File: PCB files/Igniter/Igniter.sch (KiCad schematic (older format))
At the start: 23 parts, among them IC1 74HC4050, J1 PT, J13 Micro_SD_Card, J2 PT, J3 PT, J4 PT, J5 Battery, J6 Ignition Coil +, J7 Ignition coil -, Q1 N MOSFET, SW1 ARM

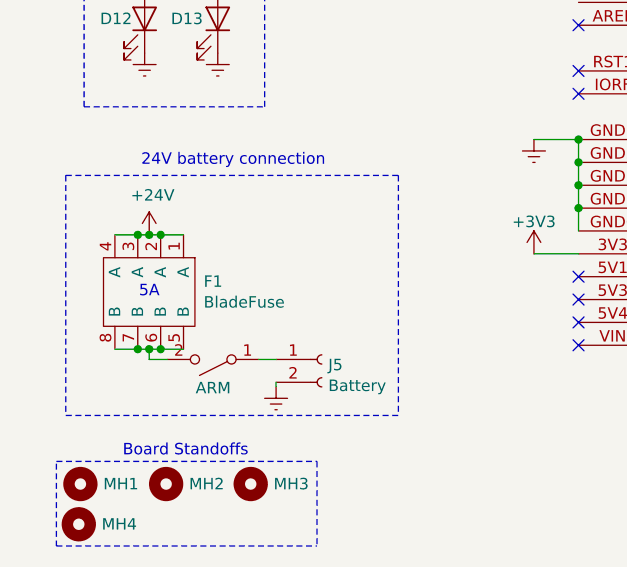
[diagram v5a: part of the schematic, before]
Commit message: 12/17/2019
-Board layout changes to make better routing paths, no traces drawn yet
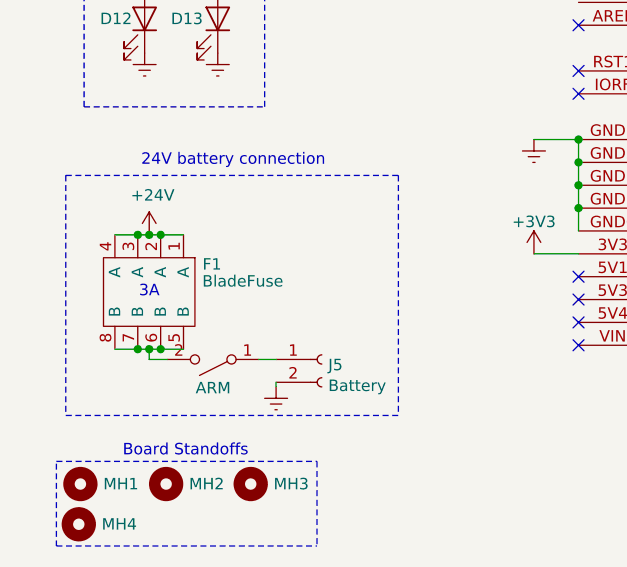
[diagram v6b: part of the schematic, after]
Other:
- note added: "3A"
- note removed: "5A"
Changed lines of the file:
@@
 	1526 7104 1601 7104
 Text Notes 1001 6839 0    50   ~ 0
-5A
-$Comp
-L power:+24V #PWR01
-U 1 1 5DBB64EE
-P 1046 6559
-F 0 "#PWR01" H 1046 6409 50  0001 C CNN
-F 1 "+24V" H 1061 6732 50  0000 C CNN
-F 2 "" H 1046 6559 50  0001 C CNN
-F 3 "" H 1046 6559 50  0001 C CNN
-	1    1046 6559
-	1    0    0    -1
-$EndComp
+3A
 $Comp
 L power:+24V #PWR08
@@
 U 1 1 5DCA7861
 P 1196 6809
-F 0 "F1" V 1150 6897 50  0000 L CNN
-F 1 "BladeFuse" V 1241 6897 50  0000 L CNN
+F 0 "F1" V 1075 6892 50  0000 L CNN
+F 1 "BladeFuse" V 1149 6891 50  0000 L CNN
 F 2 "IgniterCustom:FuseHolder" H 1196 6809 50  0001 C CNN
 F 3 "" H 1196 6809 50  0001 C CNN
@@
 Wire Wire Line
 	896  6559 996  6559
-Wire Wire Line
-	996  6559 1046 6559
 Connection ~ 996  6559
-Wire Wire Line
-	1046 6559 1096 6559
-Connection ~ 1046 6559
 Wire Wire Line
 	1096 6559 1196 6559
@@
 Wire Notes Line
 	4667 2560 4667 471
-$Comp
-L power:+24V #PWR0122
-U 1 1 5DFBEE1E
-P 1727 3440
-F 0 "#PWR0122" H 1727 3290 50  0001 C CNN
-F 1 "+24V" H 1727 3585 50  0000 C CNN
-F 2 "" H 1727 3440 50  0001 C CNN
-F 3 "" H 1727 3440 50  0001 C CNN
-	1    1727 3440
-	-1   0    0    -1
-$EndComp
 Text Label 2924 4042 2    50   ~ 0
 PT0
@@
 PT3
 $Comp
+L Connector:Conn_01x02_Female J5
+U 1 1 5DF0B34B
+P 1801 7104
+F 0 "J5" H 1829 7080 50  0000 L CNN
+F 1 "Battery" H 1829 6989 50  0000 L CNN
+F 2 "Connector_Molex:Molex_Mini-Fit_Jr_5566-02A_2x01_P4.20mm_Vertical" H 1801 7104 50  0001 C CNN
+F 3 "~" H 1801 7104 50  0001 C CNN
+	1    1801 7104
+	1    0    0    -1
+$EndComp
+Wire Wire Line
+	1046 6559 1096 6559
+Wire Wire Line
+	996  6559 1046 6559
+Connection ~ 1046 6559
+$Comp
+L power:+24V #PWR01
+U 1 1 5DBB64EE
+P 1046 6559
+F 0 "#PWR01" H 1046 6409 50  0001 C CNN
+F 1 "+24V" H 1061 6732 50  0000 C CNN
+F 2 "" H 1046 6559 50  0001 C CNN
+F 3 "" H 1046 6559 50  0001 C CNN
+	1    1046 6559
+	1    0    0    -1
+$EndComp
+$Comp
 L power:+24V #PWR0123
 U 1 1 5DFC5913
@@
 $EndComp
 $Comp
+L power:+24V #PWR0125
+U 1 1 5DFD3DEC
+P 2260 4037
+F 0 "#PWR0125" H 2260 3887 50  0001 C CNN
+F 1 "+24V" H 2260 4182 50  0000 C CNN
+F 2 "" H 2260 4037 50  0001 C CNN
+F 3 "" H 2260 4037 50  0001 C CNN
+	1    2260 4037
+	-1   0    0    -1
+$EndComp
+$Comp
 L power:+24V #PWR0124
 U 1 1 5DFD2F0A
@@
 $EndComp
 $Comp
-L power:+24V #PWR0125
-U 1 1 5DFD3DEC
-P 2260 4037
-F 0 "#PWR0125" H 2260 3887 50  0001 C CNN
-F 1 "+24V" H 2260 4182 50  0000 C CNN
-F 2 "" H 2260 4037 50  0001 C CNN
-F 3 "" H 2260 4037 50  0001 C CNN
-	1    2260 4037
+L power:+24V #PWR0122
+U 1 1 5DFBEE1E
+P 1727 3440
+F 0 "#PWR0122" H 1727 3290 50  0001 C CNN
+F 1 "+24V" H 1727 3585 50  0000 C CNN
+F 2 "" H 1727 3440 50  0001 C CNN
+F 3 "" H 1727 3440 50  0001 C CNN
+	1    1727 3440
 	-1   0    0    -1
 $EndComp
-$Comp
-L Connector:Conn_01x02_Female J5
-U 1 1 5DF0B34B
-P 1801 7104
-F 0 "J5" H 1829 7080 50  0000 L CNN
-F 1 "Battery" H 1829 6989 50  0000 L CNN
-F 2 "Connector_Molex:Molex_Mini-Fit_Jr_5566-02A_2x01_P4.20mm_Vertical" H 1801 7104 50  0001 C CNN
-F 3 "~" H 1801 7104 50  0001 C CNN
-	1    1801 7104
-	1    0    0    -1
-$EndComp
 $EndSCHEMATC

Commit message: 12/18/2019
-Changed Solenoid connector to SPOX
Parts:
- D12: value 3V3_GOOD -> 3V3
- D13: value 24V_ARMED -> 24V
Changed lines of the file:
@@
 AR Path="/5DAC3A7D" Ref="D13"  Part="1"
 F 0 "D13" V 1346 5549 50  0000 R CNN
-F 1 "24V_ARMED" V 1293 5497 50  0001 R CNN
+F 1 "24V" V 1293 5497 50  0001 R CNN
 F 2 "LED_SMD:LED_1206_3216Metric" H 1346 5614 50  0001 C CNN
 F 3 "~" H 1346 5614 50  0001 C CNN
@@
 AR Path="/5DC81323" Ref="D12"  Part="1"
 F 0 "D12" V 1026 5559 50  0000 R CNN
-F 1 "3V3_GOOD" V 973 5497 50  0001 R CNN
+F 1 "3V3" V 973 5497 50  0001 R CNN
 F 2 "LED_SMD:LED_1206_3216Metric" H 1026 5614 50  0001 C CNN
 F 3 "~" H 1026 5614 50  0001 C CNN

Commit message: 1/5/2020
-Fixed mounting hole size
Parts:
- MH1, MH2, MH3, MH4: footprint MountingHole:MountingHole_2.2mm_M2 -> MountingHole:MountingHole_3.5mm
- Q1: footprint Package_TO_SOT_SMD:SOT-223 -> Package_TO_SOT_SMD:SOT-23_Handsoldering
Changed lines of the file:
@@
 F 0 "MH2" H 1220 7649 50  0000 L CNN
 F 1 "MountingHole" H 1220 7604 50  0001 L CNN
-F 2 "MountingHole:MountingHole_2.2mm_M2" H 1120 7649 50  0001 C CNN
+F 2 "MountingHole:MountingHole_3.5mm" H 1120 7649 50  0001 C CNN
 F 3 "~" H 1120 7649 50  0001 C CNN
 	1    1120 7649
@@
 F 0 "MH1" H 645 7649 50  0000 R CNN
 F 1 "MountingHole" H 845 7604 50  0001 L CNN
-F 2 "MountingHole:MountingHole_2.2mm_M2" H 745 7649 50  0001 C CNN
+F 2 "MountingHole:MountingHole_3.5mm" H 745 7649 50  0001 C CNN
 F 3 "~" H 745 7649 50  0001 C CNN
 	1    745  7649
@@
 F 0 "MH3" H 1590 7649 50  0000 L CNN
 F 1 "MountingHole" H 1590 7604 50  0001 L CNN
-F 2 "MountingHole:MountingHole_2.2mm_M2" H 1490 7649 50  0001 C CNN
+F 2 "MountingHole:MountingHole_3.5mm" H 1490 7649 50  0001 C CNN
 F 3 "~" H 1490 7649 50  0001 C CNN
 	1    1490 7649
@@
 F 0 "Q1" H 8272 3887 50  0000 L CNN
 F 1 "N MOSFET" H 8272 3841 50  0001 L CNN
-F 2 "Package_TO_SOT_SMD:SOT-223" H 8266 3941 50  0001 C CNN
+F 2 "Package_TO_SOT_SMD:SOT-23_Handsoldering" H 8266 3941 50  0001 C CNN
 F 3 "~" H 8066 3841 50  0001 C CNN
 	1    8066 3841
@@
 F 0 "MH4" H 838 7825 50  0000 L CNN
 F 1 "MountingHole" H 838 7780 50  0001 L CNN
-F 2 "MountingHole:MountingHole_2.2mm_M2" H 738 7825 50  0001 C CNN
+F 2 "MountingHole:MountingHole_3.5mm" H 738 7825 50  0001 C CNN
 F 3 "~" H 738 7825 50  0001 C CNN
 	1    738  7825
